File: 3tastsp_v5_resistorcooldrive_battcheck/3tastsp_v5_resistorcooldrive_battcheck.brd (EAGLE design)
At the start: 86.4 x 61 mm, 27 parts, among them X1 2516-

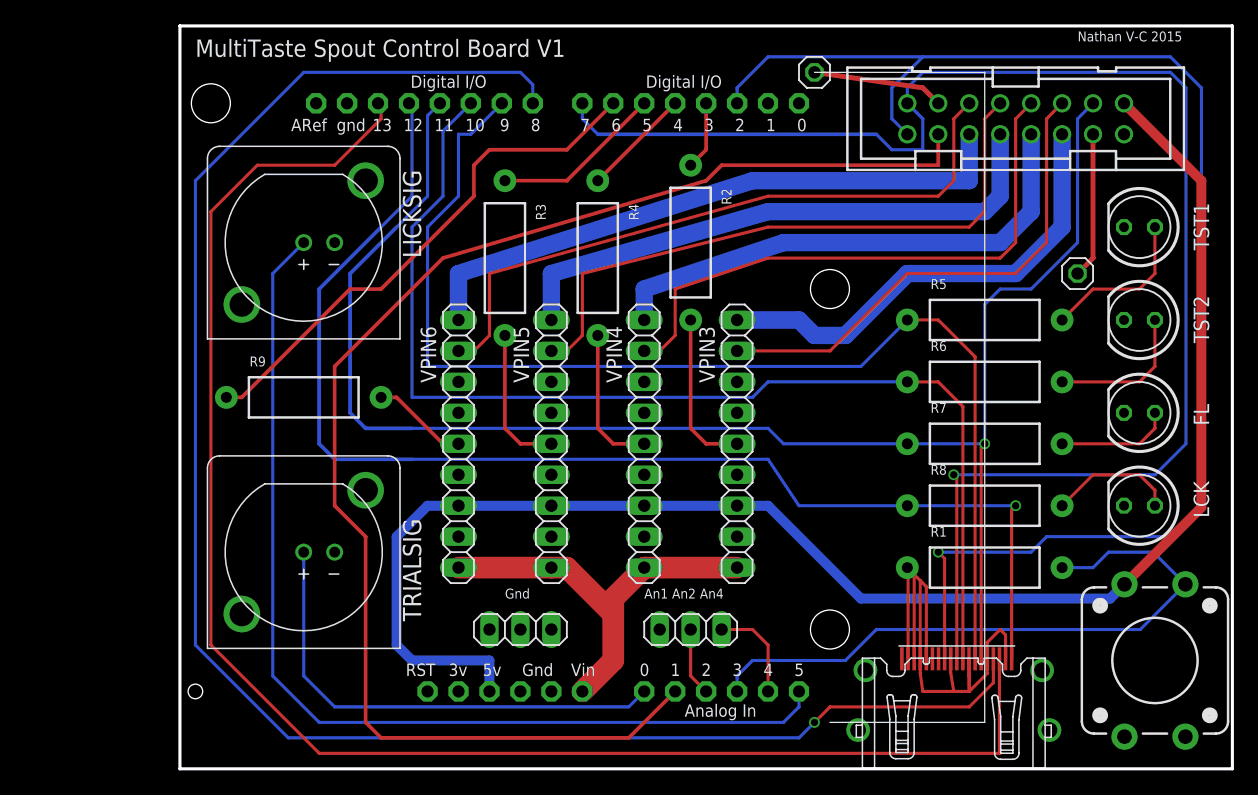
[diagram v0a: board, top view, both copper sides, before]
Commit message: Update PCBs, add IR option
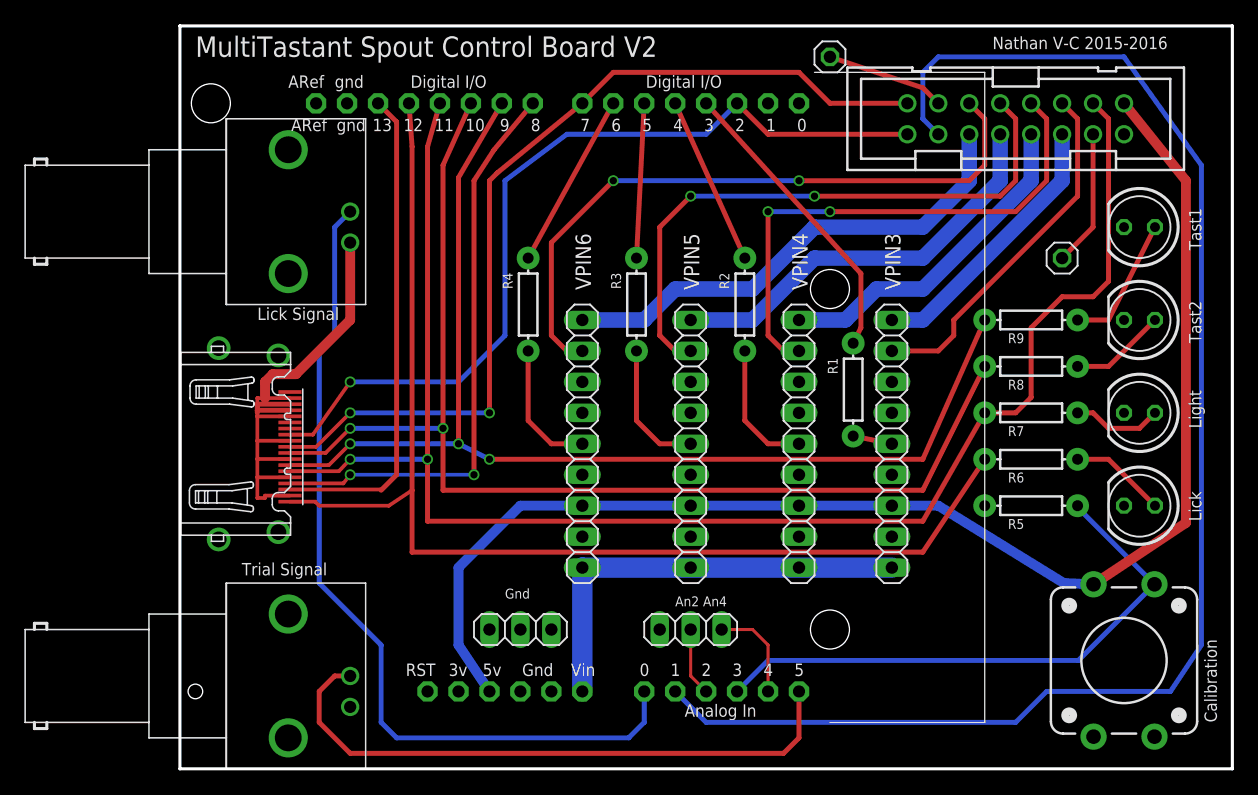
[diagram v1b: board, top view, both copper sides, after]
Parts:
- LICKSIG, TRIALSIG: value BNC_VERTICAL -> BNC_RIGHT_ANGLE; device open-ephys:BNC_VERTICAL -> connectors:BNC_RIGHT_ANGLE
- R1, R2, R3, R4, R5, R6, R7, R8, R9: device SparkFun-Resistors:AXIAL-0.5 -> SparkFun-Resistors:AXIAL-0.3EZ
- moved U$10 62.3 mm to (5.08, 26.7), turned to 270 degrees
- moved R9 60.0 mm to (69.8, 36.8)
- moved R1 18.2 mm to (55.2, 31.1), turned to 270 degrees
- moved R5 15.7 mm to (69.8, 21.6)
- moved VPIN3 12.7 mm to (58.4, 26.7)
- moved TRIALSIG 12.7 mm to (2.54, 7.62), turned to 90 degrees
- moved VPIN4 12.7 mm to (50.8, 26.7)
- moved R8 12.0 mm to (69.8, 33.0)
- moved R3 11.4 mm to (37.5, 38.1)
- moved VPIN5 11.4 mm to (41.9, 26.7)
- moved VPIN6 10.2 mm to (33.0, 26.7)
- moved LICKSIG 8.03 mm to (2.54, 45.7), turned to 90 degrees
- moved R6 7.41 mm to (69.8, 25.4)
- moved R4 6.87 mm to (28.6, 38.1)
- moved R2 6.75 mm to (46.4, 38.1)
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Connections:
- net D10: now also R9.P$1; no longer R5.P$1
- net D11: now also R8.P$1; no longer R6.P$1
- net D7: now also R6.P$1; no longer R8.P$1
- net GND: now also LICKSIG.P$GND, R5.P$1, TRIALSIG.P$GND; no longer LICKSIG.P$2, R1.P$1, TRIALSIG.P$2
- net N$12: now also R2.P$2; no longer R4.P$2
- net N$13: now also R4.P$1; no longer R9.P$1
- net N$15: now also R2.P$1; no longer R4.P$1
- net N$16: now also R1.P$1; no longer R2.P$1
- net N$18: now also R5.P$2; no longer R1.P$2
- net N$2: now also TRIALSIG.P$SIG; no longer LICKSIG.P$1
- net N$29: now also R4.P$2; no longer R9.P$2
- net N$3: now also LICKSIG.P$SIG; no longer TRIALSIG.P$1
- net N$4: now also R6.P$2; no longer R8.P$2
- net N$7: now also R8.P$2; no longer R6.P$2
- net N$8: now also R9.P$2; no longer R5.P$2
- net N$9: now also R1.P$2; no longer R2.P$2
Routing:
- net D8: track 143.9 -> 47.6 mm, vias 1 -> 2
- net D6: track 130.3 -> 40.4 mm
- net D12: track 124.3 -> 75.3 mm, vias 1 -> 2
- net D13: track 115.8 -> 70.6 mm
- net N$2: track 83.2 -> 50.4 mm
- net N$3: track 39.7 -> 70.2 mm
- net N$13: track 43.2 -> 14.5 mm
- net N$16: track 5.61 -> 24.7 mm
- net N$1: track 128.7 -> 112.3 mm
- net N$21: track 38.5 -> 22.5 mm
- net N$23: track 42.3 -> 27.6 mm
- net N$24: track 47.0 -> 33.9 mm
- net N$20: track 41.0 -> 29.4 mm
- net N$27: track 50.7 -> 40.3 mm
- net N$9: track 13.2 -> 3.24 mm
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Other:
- board text added: "ARef"
- board text added: "An2 An4"
- board text added: "Calibration"
- board text added: "Lick"
- board text added: "Lick Signal"
- board text added: "Light"
- board text added: "MultiTastant Spout Control Board V2"
- board text added: "Nathan V-C 2015-2016"
- board text added: "R1"
- board text added: "R2"
- board text added: "R3"
- board text added: "R4"
- board text added: "R5"
- board text added: "R6"
- board text added: "R7"
- board text added: "R8"
- board text added: "R9"
- board text added: "Tast1"
- board text added: "Tast2"
- board text added: "Trial Signal"
- board text added: "gnd"
- board text removed: "An1 An2 An4"
- board text removed: "MultiTaste Spout Control Board V1"
- board text removed: "Nathan V-C 2015"
